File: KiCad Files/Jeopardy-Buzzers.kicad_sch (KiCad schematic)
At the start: 24 parts, among them J1 USB_C_Receptacle_USB2.0_14P, J2 Conn_01x02_Pin, J3 Conn_01x03_Socket, J4 Conn_01x03_Socket, J5 Conn_02x04_Odd_Even, U1 CH32V003FxUx, U2 CH340N, U3 NRF24L01_Breakout, U5 AMS1117-3.3, Y1 Crystal_24MHz

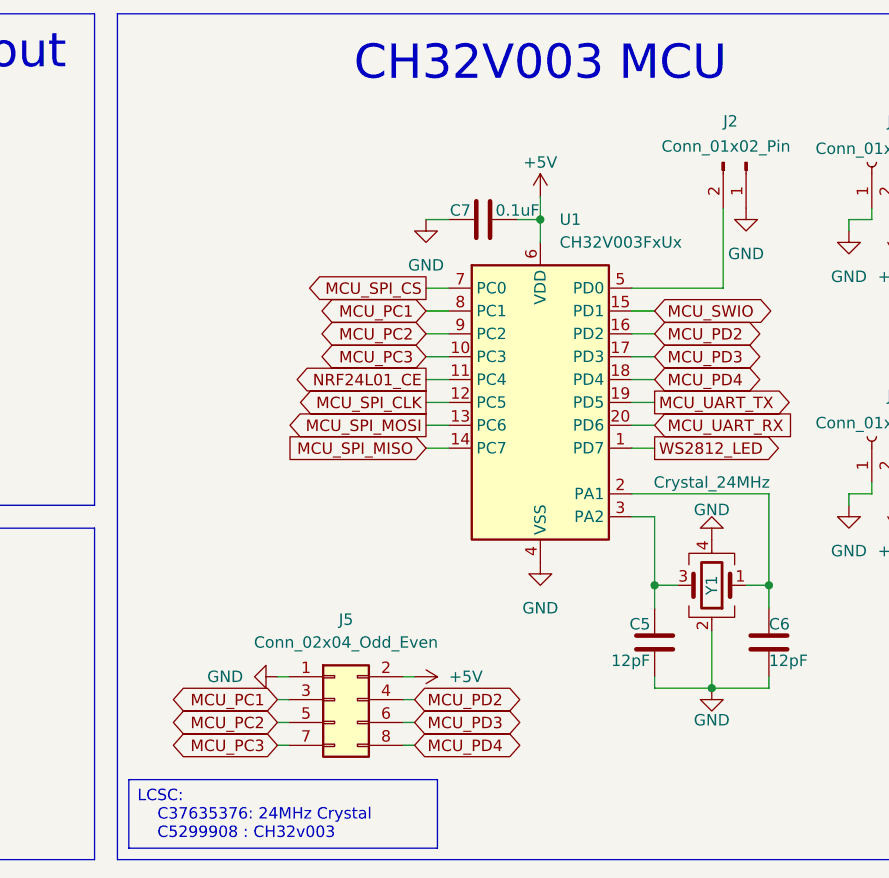
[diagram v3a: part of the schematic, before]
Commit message: moved parts around and started placing planes
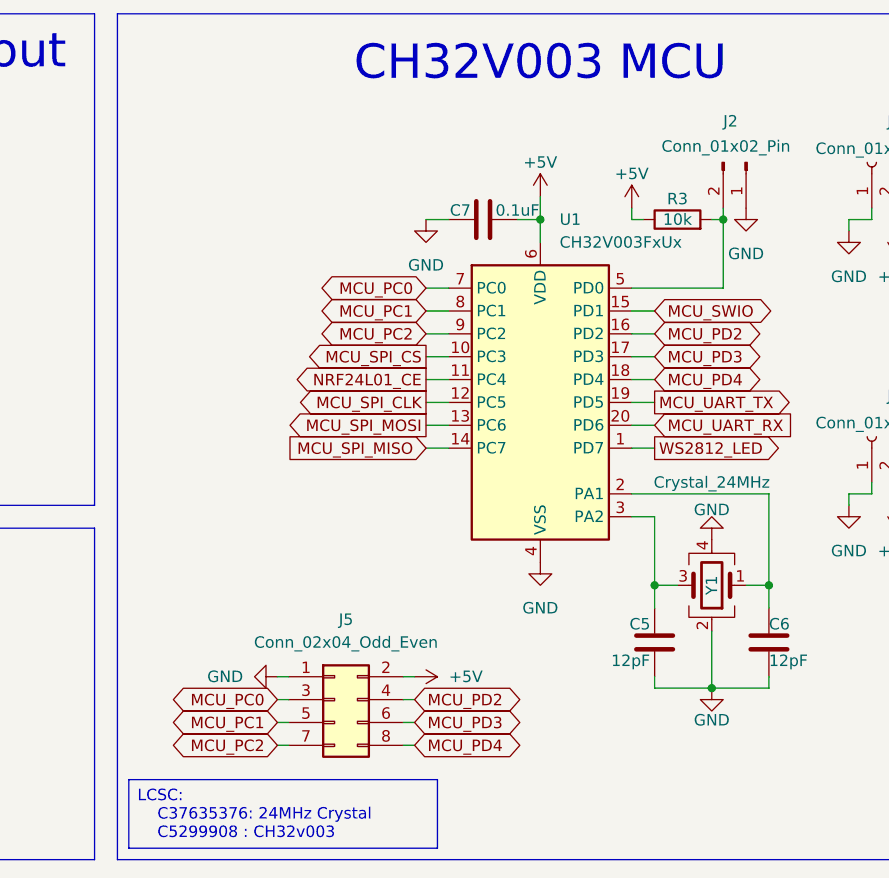
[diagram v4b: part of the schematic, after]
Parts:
- added R3: 10k, Resistor_SMD:R_0603_1608Metric_Pad0.98x0.95mm_HandSolder, symbol Device:R
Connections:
- net +5V: now also R3.1
- net MCU_PC1: now also J5.5 (Pin_5); no longer J5.3 (Pin_3)
- net MCU_PC2: now also J5.7 (Pin_7); no longer J5.5 (Pin_5)
- net MCU_SPI_CS: now also U1.10 (PC3); no longer U1.7 (PC0)
- net at J2.2 (Pin_2), U1.5 (PD0): now also R3.2
- removed net MCU_PC3: J5.7 (Pin_7), U1.10 (PC3)
- new net MCU_PC0: J5.3 (Pin_3), U1.7 (PC0)
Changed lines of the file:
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@@
 		(color 0 0 0 0)
 	)
+	(junction
+		(at 142.24 36.83)
+		(diameter 0)
+		(color 0 0 0 0)
+	)
 	(no_connect
 		(at 193.04 55.88)
@@
 	(wire
 		(pts
+			(xy 142.24 36.83) (xy 142.24 44.45)
+		)
+		(stroke
+			(width 0)
+			(type default)
+		)
+	)
+	(wire
+		(pts
 			(xy 132.08 52.07) (xy 134.62 52.07)
 		)
@@
 	(wire
 		(pts
+			(xy 132.08 36.83) (xy 132.08 35.56)
+		)
+		(stroke
+			(width 0)
+			(type default)
+		)
+	)
+	(wire
+		(pts
 			(xy 132.08 49.53) (xy 134.62 49.53)
 		)
@@
 	(wire
 		(pts
+			(xy 133.35 36.83) (xy 132.08 36.83)
+		)
+		(stroke
+			(width 0)
+			(type default)
+		)
+	)
+	(wire
+		(pts
 			(xy 223.52 55.88) (xy 223.52 64.77)
 		)
@@
 	(wire
 		(pts
+			(xy 140.97 36.83) (xy 142.24 36.83)
+		)
+		(stroke
+			(width 0)
+			(type default)
+		)
+	)
+	(wire
+		(pts
 			(xy 147.32 77.47) (xy 147.32 80.01)
 		)
@@
 	(wire
 		(pts
-			(xy 142.24 35.56) (xy 142.24 44.45)
+			(xy 142.24 35.56) (xy 142.24 36.83)
 		)
 		(stroke
@@
 		)
 	)
-	(global_label "MCU_PC1"
+	(global_label "MCU_PC2"
 		(shape bidirectional)
-		(at 92.71 90.17 180)
+		(at 92.71 95.25 180)
 		(fields_autoplaced yes)
 		(effects
@@
 		)
 		(property "Intersheetrefs" "${INTERSHEET_REFS}"
-			(at 79.8445 90.17 0)
+			(at 79.8445 95.25 0)
 			(effects
 				(font
@@
 		)
 	)
-	(global_label "MCU_PC2"
+	(global_label "MCU_PD4"
 		(shape bidirectional)
-		(at 92.71 92.71 180)
+		(at 107.95 95.25 0)
 		(fields_autoplaced yes)
 		(effects
@@
 				(size 1.27 1.27)
 			)
-			(justify right)
+			(justify left)
 		)
 		(property "Intersheetrefs" "${INTERSHEET_REFS}"
-			(at 79.8445 92.71 0)
+			(at 120.8155 95.25 0)
 			(effects
 				(font
 					(size 1.27 1.27)
 				)
-				(justify right)
+				(justify left)
 				(hide yes)
 			)
 		)
 	)
-	(global_label "MCU_PD4"
-		(shape bidirectional)
-		(at 107.95 95.25 0)
+	(global_label "MCU_SPI_CS"
+		(shape output)
+		(at 109.22 52.07 180)
 		(fields_autoplaced yes)
 		(effects
@@
 				(size 1.27 1.27)
 			)
-			(justify left)
+			(justify right)
 		)
 		(property "Intersheetrefs" "${INTERSHEET_REFS}"
-			(at 120.8155 95.25 0)
+			(at 94.6839 52.07 0)
 			(effects
 				(font
 					(size 1.27 1.27)
 				)
-				(justify left)
+				(justify right)
 				(hide yes)
 			)
@@
 		)
 	)
+	(global_label "MCU_PC0"
+		(shape bidirectional)
+		(at 92.71 90.17 180)
+		(fields_autoplaced yes)
+		(effects
+			(font
+				(size 1.27 1.27)
+			)
+			(justify right)
+		)
+		(property "Intersheetrefs" "${INTERSHEET_REFS}"
+			(at 79.8445 90.17 0)
+			(effects
+				(font
+					(size 1.27 1.27)
+				)
+				(justify right)
+				(hide yes)
+			)
+		)
+	)
 	(global_label "MCU_SWIO"
 		(shape bidirectional)
@@
 		)
 	)
-	(global_label "MCU_PC3"
-		(shape bidirectional)
-		(at 109.22 52.07 180)
-		(fields_autoplaced yes)
-		(effects
-			(font
-				(size 1.27 1.27)
-			)
-			(justify right)
-		)
-		(property "Intersheetrefs" "${INTERSHEET_REFS}"
-			(at 96.3545 52.07 0)
-			(effects
-				(font
-					(size 1.27 1.27)
-				)
-				(justify right)
-				(hide yes)
-			)
-		)
-	)
-	(global_label "MCU_PC3"
-		(shape bidirectional)
-		(at 92.71 95.25 180)
-		(fields_autoplaced yes)
-		(effects
-			(font
-				(size 1.27 1.27)
-			)
-			(justify right)
-		)
-		(property "Intersheetrefs" "${INTERSHEET_REFS}"
-			(at 79.8445 95.25 0)
-			(effects
-				(font
-					(size 1.27 1.27)
-				)
-				(justify right)
-				(hide yes)
-			)
-		)
-	)
 	(global_label "USB_D-"
 		(shape output)
@@
 		)
 	)
-	(global_label "MCU_SPI_CS"
-		(shape output)
+	(global_label "MCU_PC0"
+		(shape bidirectional)
 		(at 109.22 44.45 180)
 		(fields_autoplaced yes)
@@
 		)
 		(property "Intersheetrefs" "${INTERSHEET_REFS}"
-			(at 94.6839 44.45 0)
+			(at 96.3545 44.45 0)
+			(effects
+				(font
+					(size 1.27 1.27)
+				)
+				(justify right)
+				(hide yes)
+			)
+		)
+	)
+	(global_label "MCU_PC1"
+		(shape bidirectional)
+		(at 92.71 92.71 180)
+		(fields_autoplaced yes)
+		(effects
+			(font
+				(size 1.27 1.27)
+			)
+			(justify right)
+		)
+		(property "Intersheetrefs" "${INTERSHEET_REFS}"
+			(at 79.8445 92.71 0)
 			(effects
 				(font
@@
 	)
 	(symbol
+		(lib_id "Device:R")
+		(at 137.16 36.83 90)
+		(unit 1)
+		(exclude_from_sim no)
+		(in_bom yes)
+		(on_board yes)
+		(dnp no)
+		(property "Reference" "R3"
+			(at 137.16 34.544 90)
+			(effects
+				(font
+					(size 1.27 1.27)
+				)
+			)
+		)
+		(property "Value" "10k"
+			(at 137.16 36.83 90)
+			(effects
+				(font
+					(size 1.27 1.27)
+				)
+			)
+		)
+		(property "Footprint" "Resistor_SMD:R_0603_1608Metric_Pad0.98x0.95mm_HandSolder"
+			(at 137.16 38.608 90)
+			(effects
+				(font
+					(size 1.27 1.27)
+				)
+				(hide yes)
+			)
+		)
+		(property "Datasheet" "~"
+			(at 137.16 36.83 0)
+			(effects
+				(font
+					(size 1.27 1.27)
+				)
+				(hide yes)
+			)
+		)
+		(property "Description" "Resistor"
+			(at 137.16 36.83 0)
+			(effects
+				(font
+					(size 1.27 1.27)
+				)
+				(hide yes)
+			)
+		)
+		(pin "1"
+		)
+		(pin "2"
+		)
+		(instances
+			(project ""
+				(path "/b8afa041-22fc-49f7-96f6-f381d6de2196"
+					(reference "R3")
+					(unit 1)
+				)
+			)
+		)
+	)
+	(symbol
 		(lib_id "Device:D_Zener")
 		(at 223.52 73.66 270)
@@
 					(unit 1)
 				)
+			)
+		)
+	)
+	(symbol
+		(lib_id "power:+5V")
+		(at 132.08 35.56 0)
+		(unit 1)
+		(exclude_from_sim no)
+		(in_bom yes)
+		(on_board yes)
+		(dnp no)
+		(property "Reference" "#PWR028"
+			(at 132.08 39.37 0)
+			(effects
+				(font
+					(size 1.27 1.27)
+				)
+				(hide yes)
+			)
+		)
+		(property "Value" "+5V"
+			(at 132.08 31.75 0)
+			(effects
+				(font
+					(size 1.27 1.27)
+				)
+			)
+		)
+		(property "Footprint" ""
+			(at 132.08 35.56 0)
+			(effects
+				(font
+					(size 1.27 1.27)
+				)
+				(hide yes)
+			)
+		)
+		(property "Datasheet" ""
+			(at 132.08 35.56 0)
+			(effects
+				(font
+					(size 1.27 1.27)
+				)
+				(hide yes)
+			)
+		)
+		(property "Description" "Power symbol creates a global label with name \"+5V\""
+			(at 132.08 35.56 0)
+			(effects
+				(font
+					(size 1.27 1.27)
+				)
+				(hide yes)
+			)
+		)
+		(pin "1"
+		)
+		(instances
+			(project "Jeopardy-Buzzers"
+				(path "/b8afa041-22fc-49f7-96f6-f381d6de2196"
+					(reference "#PWR028")
+					(unit 1)
+				)

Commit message: routed most of the traces, just need to pass ERC/DRC
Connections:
- net MCU_PC0: now also J5.7 (Pin_7); no longer J5.3 (Pin_3)
- net MCU_PC2: now also J5.3 (Pin_3); no longer J5.7 (Pin_7)
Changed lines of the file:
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@@
-		)
-	)
-	(global_label "MCU_PC2"
-		(shape bidirectional)
-		(at 92.71 95.25 180)
-		(fields_autoplaced yes)
-		(effects
-			(font
-				(size 1.27 1.27)
-			)
-			(justify right)
-		)
-		(property "Intersheetrefs" "${INTERSHEET_REFS}"
-			(at 79.8445 95.25 0)
-			(effects
-				(font
-					(size 1.27 1.27)
-				)
-				(justify right)
-				(hide yes)
-			)
 		)
 	)
@@
 		)
 	)
+	(global_label "MCU_PC2"
+		(shape bidirectional)
+		(at 92.71 90.17 180)
+		(fields_autoplaced yes)
+		(effects
+			(font
+				(size 1.27 1.27)
+			)
+			(justify right)
+		)
+		(property "Intersheetrefs" "${INTERSHEET_REFS}"
+			(at 79.8445 90.17 0)
+			(effects
+				(font
+					(size 1.27 1.27)
+				)
+				(justify right)
+				(hide yes)
+			)
+		)
+	)
 	(global_label "MCU_UART_TX"
 		(shape input)
@@
 		)
 	)
-	(global_label "MCU_PC0"
-		(shape bidirectional)
-		(at 92.71 90.17 180)
-		(fields_autoplaced yes)
-		(effects
-			(font
-				(size 1.27 1.27)
-			)
-			(justify right)
-		)
-		(property "Intersheetrefs" "${INTERSHEET_REFS}"
-			(at 79.8445 90.17 0)
-			(effects
-				(font
-					(size 1.27 1.27)
-				)
-				(justify right)
-				(hide yes)
-			)
-		)
-	)
 	(global_label "MCU_SWIO"
 		(shape bidirectional)
@@
 			(effects
 				(font
+					(size 1.27 1.27)
+				)
+				(justify right)
+				(hide yes)
+			)
+		)
+	)
+	(global_label "MCU_PC0"
+		(shape bidirectional)
+		(at 92.71 95.25 180)
+		(fields_autoplaced yes)
+		(effects
+			(font
+				(size 1.27 1.27)
+			)
+			(justify right)
+		)
+		(property "Intersheetrefs" "${INTERSHEET_REFS}"
+			(at 79.8445 95.25 0)
+			(effects
+				(font

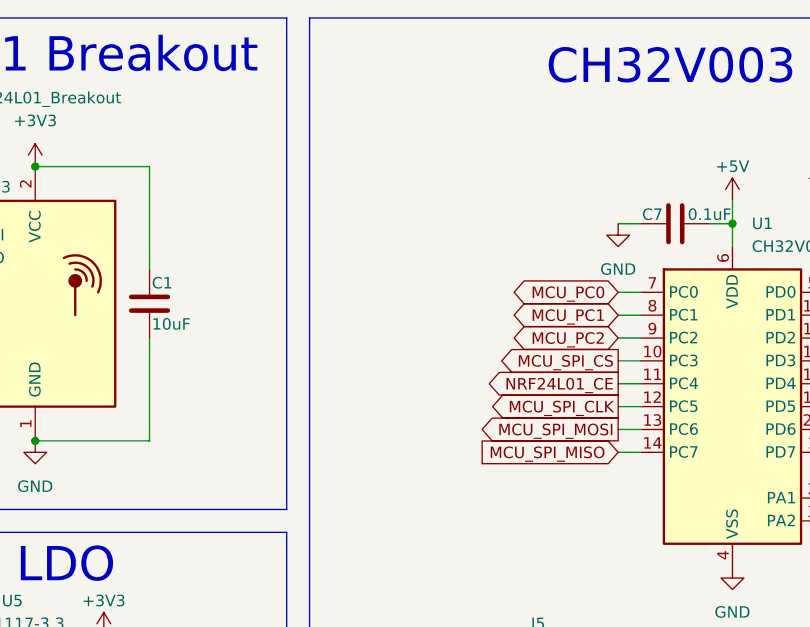
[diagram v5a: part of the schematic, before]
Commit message: Added power led and user controlled led
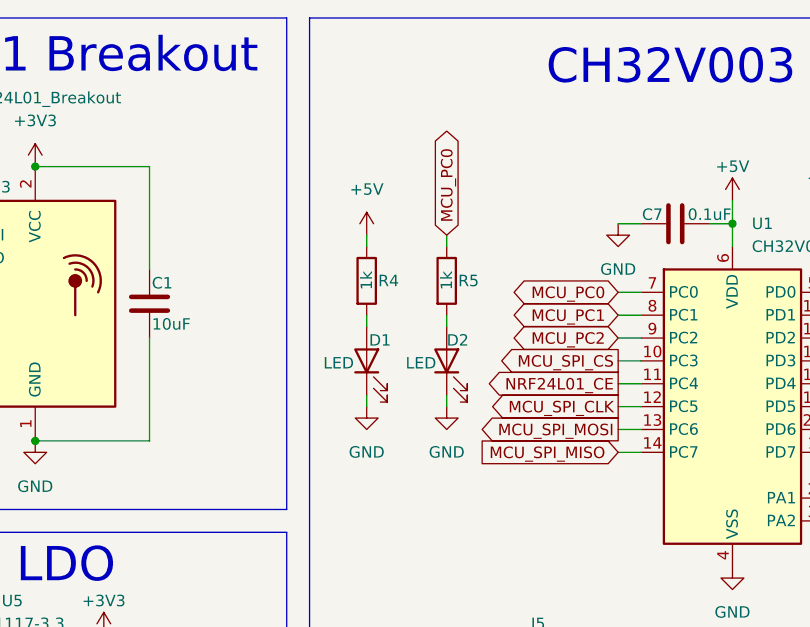
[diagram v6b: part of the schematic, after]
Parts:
- added D1, D2: LED, LED_SMD:LED_0603_1608Metric_Pad1.05x0.95mm_HandSolder, symbol Device:LED
- added R4, R5: 1k, Resistor_SMD:R_0603_1608Metric_Pad0.98x0.95mm_HandSolder, symbol Device:R
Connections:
- net +5V: now also R4.1
- net GND: now also D1.1 (K), D2.1 (K)
- net MCU_PC0: now also R5.1
- new net: D2.2 (A), R5.2
- new net: D1.2 (A), R4.2

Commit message: Updated LCSC Part Numbers
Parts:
- C1, C2: LCSC Part # (none) -> C19702
- C3: LCSC Part # (none) -> C6119863
- C4, C7: LCSC Part # (none) -> C14663
- C5, C6: LCSC Part # (none) -> C519482
- D1, D2: LCSC Part # (none) -> C965799
- D4, D5, D6: LCSC Part # (none) -> C19077401
- J1: LCSC Part # (none) -> C2988369
- J3: LCSC Part # (none) -> C157929
- J4: LCSC Part # (none) -> C6332196
- J5: LCSC Part # (none) -> C7501275
- R1, R2: LCSC Part # (none) -> C3016319
- R3: LCSC Part # (none) -> C98220
- R4, R5: LCSC Part # (none) -> C103198
- U1: LCSC Part # (none) -> C5299908
- U2: LCSC Part # (none) -> C2977777
- U3: LCSC Part # (none) -> C2834799
- U5: LCSC Part # (none) -> C5205141
- Y1: LCSC Part # (none) -> C37635376
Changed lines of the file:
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@@
 			)
 		)
+		(property "LCSC Part #" "C37635376"
+			(at 140.97 77.47 90)
+			(effects
+				(font
+					(size 1.27 1.27)
+				)
+				(hide yes)
+			)
+		)
 		(pin "1"
 		)
@@
 			)
 		)
+		(property "LCSC Part #" "C19702"
+			(at 57.15 45.72 0)
+			(effects
+				(font
+					(size 1.27 1.27)
+				)
+				(hide yes)
+			)
+		)
 		(pin "2"
 		)
@@
 			)
 		)
+		(property "LCSC Part #" "C7501275"
+			(at 99.06 90.17 0)
+			(effects
+				(font
+					(size 1.27 1.27)
+				)
+				(hide yes)
+			)
+		)
 		(pin "2"
 		)
@@
 			)
 		)
+		(property "LCSC Part #" "C14663"
+			(at 115.57 36.83 90)
+			(effects
+				(font
+					(size 1.27 1.27)
+				)
+				(hide yes)
+			)
+		)
 		(pin "2"
 		)
@@
 			)
 		)
+		(property "LCSC Part #" "C6332196"
+			(at 161.29 60.96 90)
+			(effects
+				(font
+					(size 1.27 1.27)
+				)
+				(hide yes)
+			)
+		)
 		(pin "3"
 		)
@@
 			)
 		)
+		(property "LCSC Part #" "C19077401"
+			(at 231.14 73.66 90)
+			(effects
+				(font
+					(size 1.27 1.27)
+				)
+				(hide yes)
+			)
+		)
 		(pin "2"
 		)
@@
 			)
 		)
+		(property "LCSC Part #" "C5299908"
+			(at 121.92 57.15 0)
+			(effects
+				(font
+					(size 1.27 1.27)
+				)
+				(hide yes)
+			)
+		)
 		(pin "20"
 		)
@@
 			)
 		)
+		(property "LCSC Part #" "C103198"
+			(at 90.17 43.18 0)
+			(effects
+				(font
+					(size 1.27 1.27)
+				)
+				(hide yes)
+			)
+		)
 		(pin "1"
 		)
@@
 			)
 		)
+		(property "LCSC Part #" "C103198"
+			(at 81.28 43.18 0)
+			(effects
+				(font
+					(size 1.27 1.27)
+				)
+				(hide yes)
+			)
+		)
 		(pin "1"
 		)
@@
 			)
 		)
+		(property "LCSC Part #" "C157929"
+			(at 161.29 30.48 90)
+			(effects
+				(font
+					(size 1.27 1.27)
+				)
+				(hide yes)
+			)
+		)
 		(pin "3"
 		)
@@
 			)
 		)
+		(property "LCSC Part #" "C2834799"
+			(at 44.45 45.72 0)
+			(effects
+				(font
+					(size 1.27 1.27)
+				)
+				(hide yes)
+			)
+		)
 		(pin "7"
 		)
@@
 			)
 		)
+		(property "LCSC Part #" "C519482"
+			(at 134.62 83.82 0)
+			(effects
+				(font
+					(size 1.27 1.27)
+				)
+				(hide yes)
+			)
+		)
 		(pin "1"
 		)
@@
 			)
 		)
+		(property "LCSC Part #" "C2988369"
+			(at 265.43 73.66 0)
+			(effects
+				(font
+					(size 1.27 1.27)
+				)
+				(hide yes)
+			)
+		)
 		(pin "B9"
 		)
@@
 			)
 		)
+		(property "LCSC Part #" "C6119863"
+			(at 52.07 88.9 0)
+			(effects
+				(font
+					(size 1.27 1.27)
+				)
+				(hide yes)
+			)
+		)
 		(pin "1"
 		)
@@
 			)
 		)
+		(property "LCSC Part #" "C2977777"
+			(at 203.2 60.96 0)
+			(effects
+				(font
+					(size 1.27 1.27)
+				)
+				(hide yes)
+			)
+		)
 		(pin "7"
 		)
@@
 			)
 		)
+		(property "LCSC Part #" "C14663"
+			(at 214.63 68.58 0)
+			(effects
+				(font
+					(size 1.27 1.27)
+				)
+				(hide yes)
+			)
+		)
 		(pin "1"
 		)
@@
 			)
 		)
+		(property "LCSC Part #" "C98220"
+			(at 137.16 36.83 90)
+			(effects
+				(font
+					(size 1.27 1.27)
+				)
+				(hide yes)
+			)
+		)
 		(pin "1"
 		)
@@
 			)
 		)
+		(property "LCSC Part #" "C19077401"
+			(at 223.52 73.66 90)
+			(effects
+				(font
+					(size 1.27 1.27)
+				)
+				(hide yes)
+			)
+		)
 		(pin "2"
 		)
@@
 			)
 		)
+		(property "LCSC Part #" "C965799"
+			(at 90.17 52.07 90)
+			(effects
+				(font
+					(size 1.27 1.27)
+				)
+				(hide yes)
+			)
+		)
 		(pin "1"
 		)
@@
 			)
 		)
+		(property "LCSC Part #" "C965799"
+			(at 81.28 52.07 90)
+			(effects
+				(font
+					(size 1.27 1.27)
+				)
+				(hide yes)
+			)
+		)
 		(pin "1"
 		)
@@
 			)
 		)
+		(property "LCSC Part #" "C5205141"
+			(at 41.91 85.09 0)
+			(effects
+				(font
+					(size 1.27 1.27)
+				)
+				(hide yes)
+			)
+		)
 		(pin "1"
 		)
@@
 			)
 		)
+		(property "LCSC Part #" "C3016319"
+			(at 241.3 92.71 0)
+			(effects
+				(font
+					(size 1.27 1.27)
+				)
+				(hide yes)
+			)
+		)
 		(pin "2"
 		)
@@
 			)
 		)
+		(property "LCSC Part #" "C19702"
+			(at 31.75 88.9 0)
+			(effects
+				(font
+					(size 1.27 1.27)
+				)
+				(hide yes)
+			)
+		)
 		(pin "2"
 		)
@@
 			)
 		)
+		(property "LCSC Part #" "C519482"
+			(at 147.32 83.82 0)
+			(effects
+				(font
+					(size 1.27 1.27)
+				)
+				(hide yes)
+			)
+		)
 		(pin "1"
 		)
@@
 			)
 		)
+		(property "LCSC Part #" "C19077401"
+			(at 247.65 93.98 90)
+			(effects
+				(font
+					(size 1.27 1.27)
+				)
+				(hide yes)
+			)
+		)
 		(pin "2"
 		)
@@
 			(at 234.95 92.71 0)
 			(effects
+				(font
+					(size 1.27 1.27)
+				)
+				(hide yes)
+			)
+		)
+		(property "LCSC Part #" "C3016319"
+			(at 234.95 92.71 0)
+			(effects
